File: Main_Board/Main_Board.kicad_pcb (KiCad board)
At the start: 4 copper layers, 45 x 38.4 mm, 127 parts, among them IC1 TPS25200DRVR, J1 RESET, J2 MAIN_UART, J3 Baterry input, J4 External bords interfaces, J7 Terminal, J8 Terminal, Q1 2N7002, Q10 FDN339AN, Q7 MMBT3904LT1G, Q8 FDN339AN, Q9 MMBT3904LT1G, U1 W25Q128JVS, U2 ESP32-S3-MINI-1U, U3 TPS63031DSK, U4 TPS63031DSK, U5 TLV61070ADBV, U6 SS351AT, U7 THVD1450DR

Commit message: Layout
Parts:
- moved C4 98.4 mm to (87.8, 85.4), turned to 90 degrees
- moved C6 96.4 mm to (89.5, 85.4), turned to 90 degrees
- moved C1 96.0 mm to (91.2, 85.4), turned to 90 degrees
- moved C5 88.1 mm to (100.7, 102.3), turned to -90 degrees
- moved R4 85.7 mm to (107.8, 101.6), turned to 90 degrees
- moved C2 59.8 mm to (129.6, 92.4)
- moved J3 14.8 mm to (99.1, 80.9), turned to 0 degrees
- moved C42 14.1 mm to (84.3, 103.6), turned to 135 degrees
- moved C16 13.4 mm to (79.6, 101.4), turned to 180 degrees
- moved R33 13.4 mm to (95.6, 83.4), turned to 90 degrees
- moved C13 13.2 mm to (80.6, 91.3), turned to 90 degrees
- moved C15 12.8 mm to (78.8, 99.0), turned to -90 degrees
- moved C10 12.7 mm to (85.4, 88.2), turned to 180 degrees
- moved C34 12.4 mm to (98.1, 84.1), turned to 0 degrees
- moved C35 11.8 mm to (100.9, 84.7), turned to 90 degrees
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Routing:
- net Net-(U2-IO18): track 0.00 -> 10.2 mm
- net Net-(U2-IO17): track 0.00 -> 9.42 mm
- net /MODBUS_RX: track 1.57 -> 10.8 mm
- net /ESP32/ESP32_EN: track 8.27 -> 1.86 mm
- net /MODBUS_DIR: track 7.00 -> 0.65 mm
- net /MODBUS_TX: track 2.24 -> 7.34 mm
- net /MODBUS_RST: track 1.97 -> 0.00 mm
- net +3V3_MB: track 4.54 -> 6.45 mm

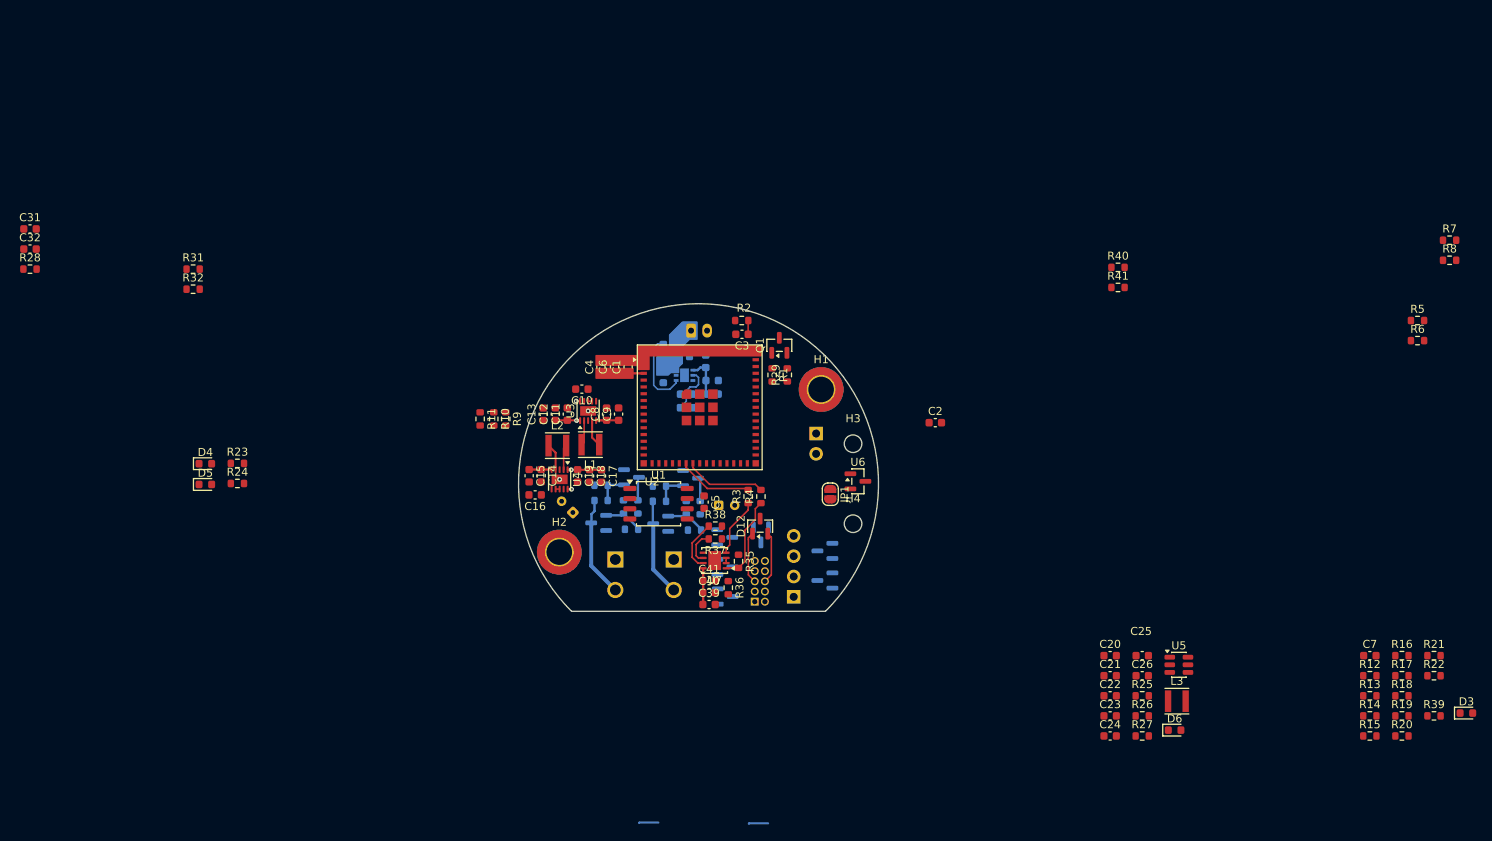
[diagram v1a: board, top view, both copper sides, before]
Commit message: Input resistors, PRG, pour zones
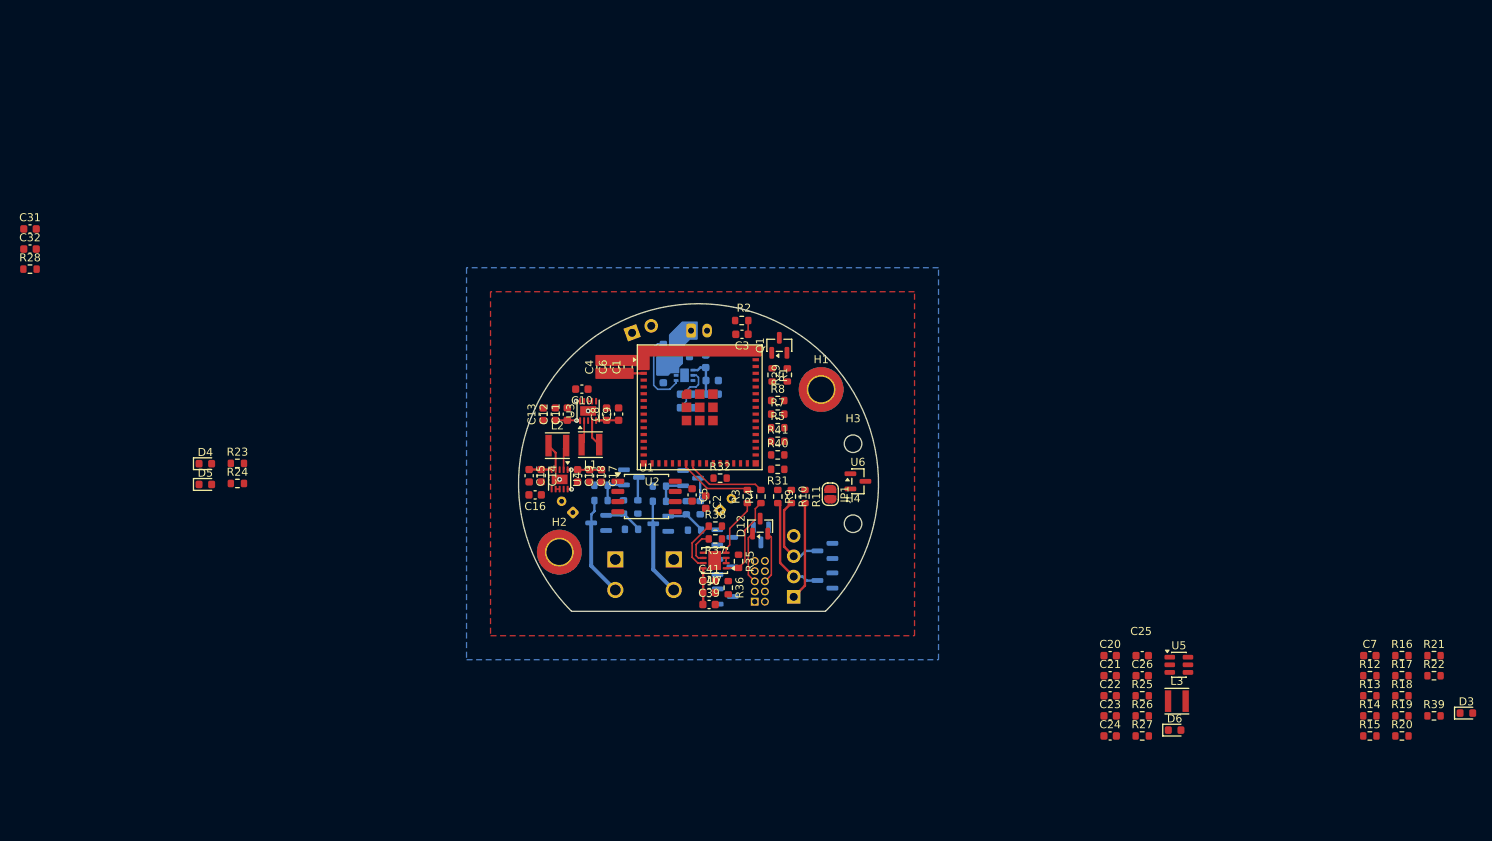
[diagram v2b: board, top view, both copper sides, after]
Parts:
- removed R6: 100R, Resistor_SMD:R_0603_1608Metric
- moved R7 86.8 mm to (109.9, 91.3)
- moved R8 85.8 mm to (109.9, 89.6)
- moved R5 81.1 mm to (109.9, 93.0)
- moved R31 77.2 mm to (109.9, 98.2), turned to 180 degrees
- moved R32 70.0 mm to (102.7, 99.3)
- moved R40 48.6 mm to (109.9, 96.4)
- moved R41 46.7 mm to (109.9, 94.7)
- moved R11 41.7 mm to (113.3, 101.6)
- moved R10 38.4 mm to (111.6, 101.6)
- moved R9 35.4 mm to (109.9, 101.6)
- moved C2 30.4 mm to (100.9, 102.3), turned to -90 degrees
- moved J1 26.2 mm to (91.7, 81.1), turned to -70 degrees
- moved U1 1.75 mm to (93.5, 101.6)
- moved C5 1.75 mm to (99.2, 101.4)
- moved C43 0.61 mm to (102.7, 103.3), turned to 45 degrees
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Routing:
- net Net-(J2-Pin_2): track 0.00 -> 13.2 mm
- net Net-(J2-Pin_1): track 0.00 -> 12.3 mm
- net Net-(J2-Pin_3): track 0.00 -> 10.7 mm
- net /PSU/Back_Boost2/V_out: track 7.19 -> 4.74 mm
- net /PSU/Back_Boost1/V_out: track 6.06 -> 3.61 mm
- added copper zone on In2.Cu, net +3V3_MB
- added copper zone on B.Cu, net GND
- added copper zone on F.Cu, net GND
- added copper zone on In1.Cu, net GND

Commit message: TVS
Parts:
- moved D8 6.88 mm to (102.2, 110.5), turned to 0 degrees
- moved D10 3.75 mm to (107.0, 106.3), turned to -90 degrees
- moved D9 3.70 mm to (103.2, 106.7)
- moved D2 1.12 mm to (115.6, 113.2), turned to -135 degrees
- moved D7 1.04 mm to (102.3, 114.0)
- moved D1 0.88 mm to (116.1, 109.2), turned to -135 degrees
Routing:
- net +5V: track 0.00 -> 5.43 mm
- net Net-(J4-Pin_3): track 0.00 -> 5.11 mm
- net Net-(J4-Pin_1): track 0.00 -> 4.08 mm
- net +3V3: track 0.00 -> 2.47 mm
- net Net-(J2-Pin_2): track 13.2 -> 14.0 mm
- net Net-(J2-Pin_3): track 10.7 -> 11.4 mm

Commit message: Layout fix, group parts
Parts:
- moved R28 150.4 mm to (160.0, 118.1)
- moved R19 136.0 mm to (74.5, 54.0)
- moved R22 135.5 mm to (74.5, 56.5)
- moved R20 131.0 mm to (84.8, 50.8)
- moved R21 116.4 mm to (99.3, 51.0)
- moved R26 101.8 mm to (84.8, 55.8)
- moved C31 96.0 mm to (111.2, 52.8)
- moved C32 96.0 mm to (111.2, 55.3)
- moved R18 94.9 mm to (141.1, 44.0)
- moved R12 94.8 mm to (121.4, 52.7)
- moved R13 94.8 mm to (121.4, 55.2)
- moved R15 94.2 mm to (135.8, 50.6)
- moved D3 90.9 mm to (146.6, 52.4)
- moved R25 90.1 mm to (99.3, 56.0)
- moved C7 87.8 mm to (135.8, 48.1)
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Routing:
- net Net-(J4-Pin_1): track 4.08 -> 3.16 mm
- net /Interfaces/B_RS485: track 6.48 -> 7.11 mm
- net /Interfaces/A_RS485: track 6.51 -> 7.10 mm
- net Net-(J4-Pin_3): track 5.11 -> 4.53 mm

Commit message: Layout
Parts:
- moved R29 48.8 mm to (150.7, 114.9)
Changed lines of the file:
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@@
 	(footprint "Resistor_SMD:R_0603_1608Metric"
 		(layer "F.Cu")
-		(at 111.1 86.4 90)
+		(at 150.7 114.9 90)
 		(descr "Resistor SMD 0603 (1608 Metric), square (rectangular) end terminal, IPC-7351 nominal, (Body size source: IPC-SM-782 page 72, https://www.pcb-3d.com/wordpress/wp-content/uploads/ipc-sm-782a_amendment_1_and_2.pdf)")
 		(tags "resistor")

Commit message: Boost layout part 1
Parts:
- moved C25 13.8 mm to (169.3, 121.5)
- moved C26 13.8 mm to (169.2, 123.0)
- moved R28 13.7 mm to (173.7, 117.7), turned to -90 degrees
- moved C21 13.3 mm to (163.6, 118.7), turned to 180 degrees
- moved C20 13.0 mm to (163.6, 117.0), turned to 180 degrees
- moved C22 11.7 mm to (162.4, 122.3), turned to -90 degrees
- moved U5 4.96 mm to (165.0, 122.9), turned to 90 degrees
- moved L3 4.31 mm to (159.3, 122.9), turned to -90 degrees

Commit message: Fix boost schematic +layout
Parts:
- moved R29 27.4 mm to (172.4, 131.7), turned to 0 degrees
- moved C23 22.0 mm to (172.4, 122.3), turned to -90 degrees
- moved C24 21.4 mm to (170.8, 122.3), turned to -90 degrees
- moved R27 18.6 mm to (168.4, 118.2)
- moved D6 13.1 mm to (172.4, 133.3)
- moved R28 5.78 mm to (168.3, 119.9), turned to 180 degrees
- moved C20 1.91 mm to (165.0, 118.3), turned to 0 degrees
- moved C21 1.84 mm to (165.0, 119.9), turned to 0 degrees
- moved C26 1.75 mm to (167.6, 122.3), turned to -90 degrees
- moved C25 0.81 mm to (169.2, 122.3), turned to -90 degrees
- moved L3 0.30 mm to (159.6, 122.9), turned to 90 degrees
- moved C22 0.20 mm to (162.4, 122.5)
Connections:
- L3 pad 1: /PSU/Boost/V_out -> Net-(U5-SW)
- L3 pad 2: Net-(U5-SW) -> /PSU/Back_Boost1/V_In
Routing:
- net GND: track 0.00 -> 11.4 mm, vias 2 -> 5
- net Net-(U5-SW): track 0.00 -> 4.52 mm
- net Net-(U5-V_{FB}): track 0.00 -> 4.24 mm
- net /PSU/Back_Boost1/V_In: track 12.5 -> 16.0 mm

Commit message: PWR layout
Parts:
- moved C23 87.4 mm to (86.7, 105.3), turned to 90 degrees
- moved C24 84.3 mm to (88.3, 105.3), turned to 90 degrees
- moved C25 81.1 mm to (89.9, 105.3), turned to 90 degrees
- moved R27 80.0 mm to (89.1, 107.6), turned to 180 degrees
- moved C26 78.0 mm to (91.5, 105.3), turned to 90 degrees
- moved R28 77.7 mm to (91.5, 108.4), turned to 90 degrees
- moved U5 73.0 mm to (93.9, 106.3), turned to -90 degrees
- moved C21 71.9 mm to (93.9, 109.3), turned to 180 degrees
- moved C20 71.5 mm to (93.9, 110.9), turned to 180 degrees
- moved C22 67.7 mm to (96.5, 106.7), turned to 90 degrees
- moved L3 62.6 mm to (99.2, 106.3), turned to -90 degrees
- moved C2 28.5 mm to (124.1, 85.7)
- moved C5 28.1 mm to (122.5, 85.7)
- moved C16 16.8 mm to (89.5, 87.9), turned to 0 degrees
- moved C15 14.4 mm to (90.2, 90.3), turned to 90 degrees
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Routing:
- net /MODBUS_RX: track 10.8 -> 0.00 mm
- net /MODBUS_TX: track 7.34 -> 0.32 mm
- net /PSU/Boost/V_out: track 0.00 -> 5.79 mm
- net GND: track 11.4 -> 14.9 mm, vias 5 -> 8
- net Net-(U5-V_{FB}): track 4.24 -> 3.05 mm
